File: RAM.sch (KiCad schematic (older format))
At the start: 1 part, among them IC1 EP4CE10F17

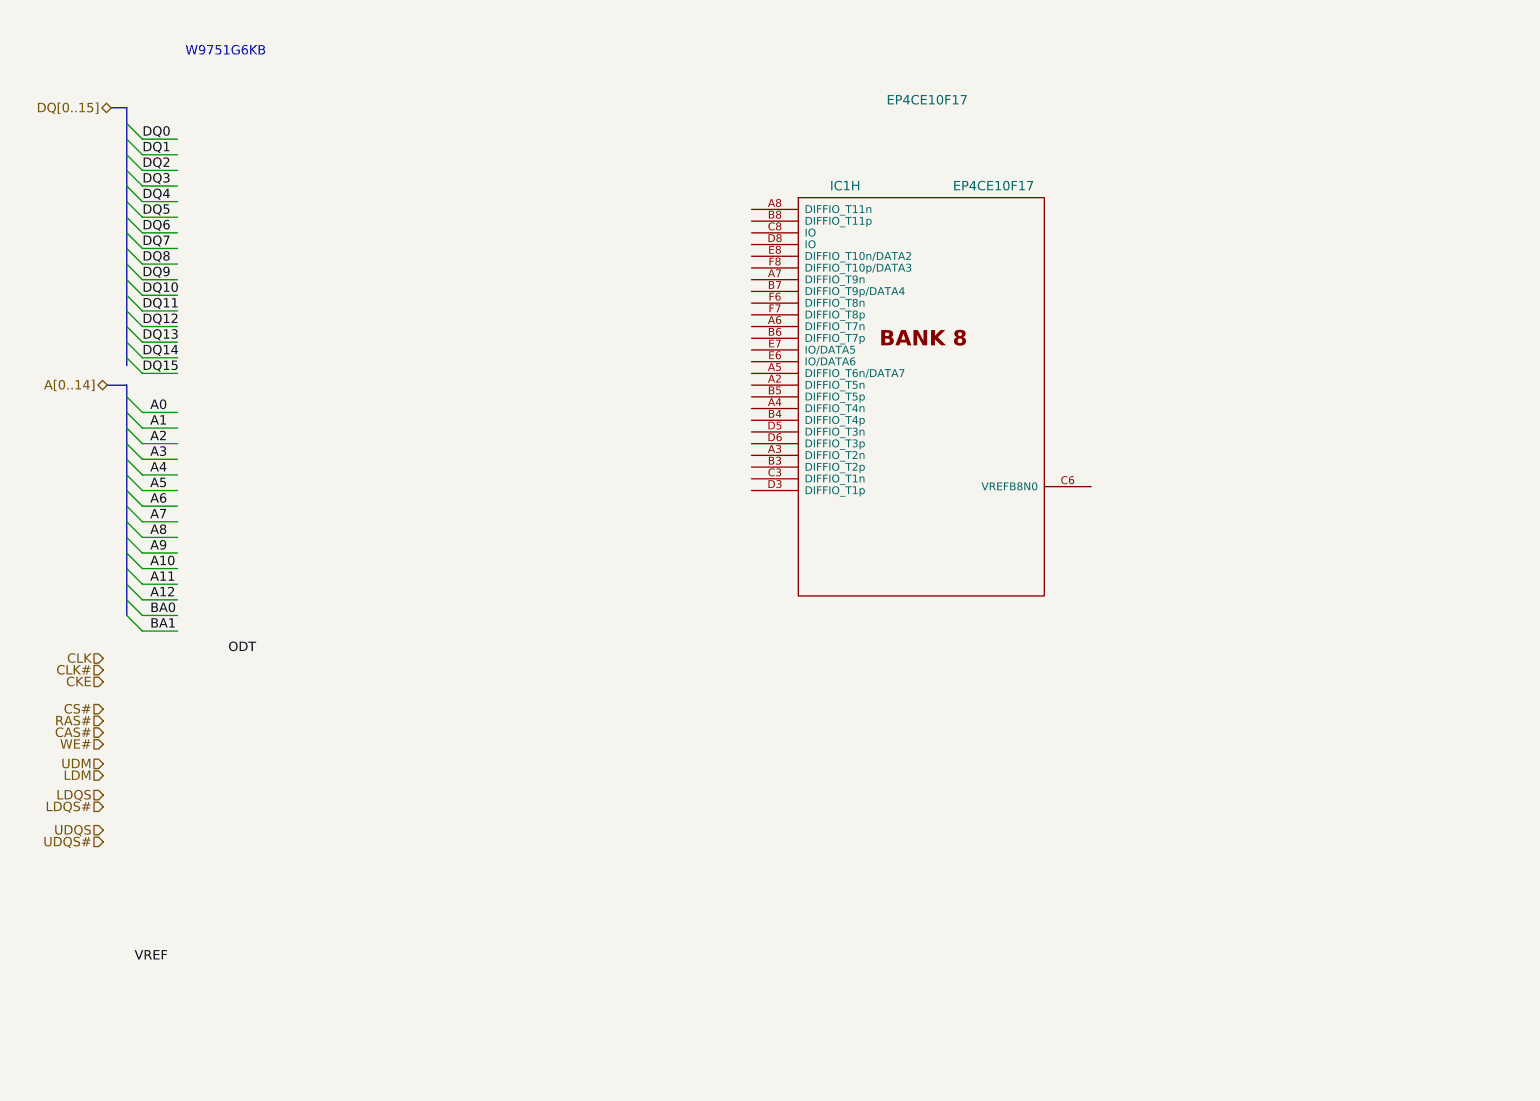
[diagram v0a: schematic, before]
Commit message: Start fitting DDR2
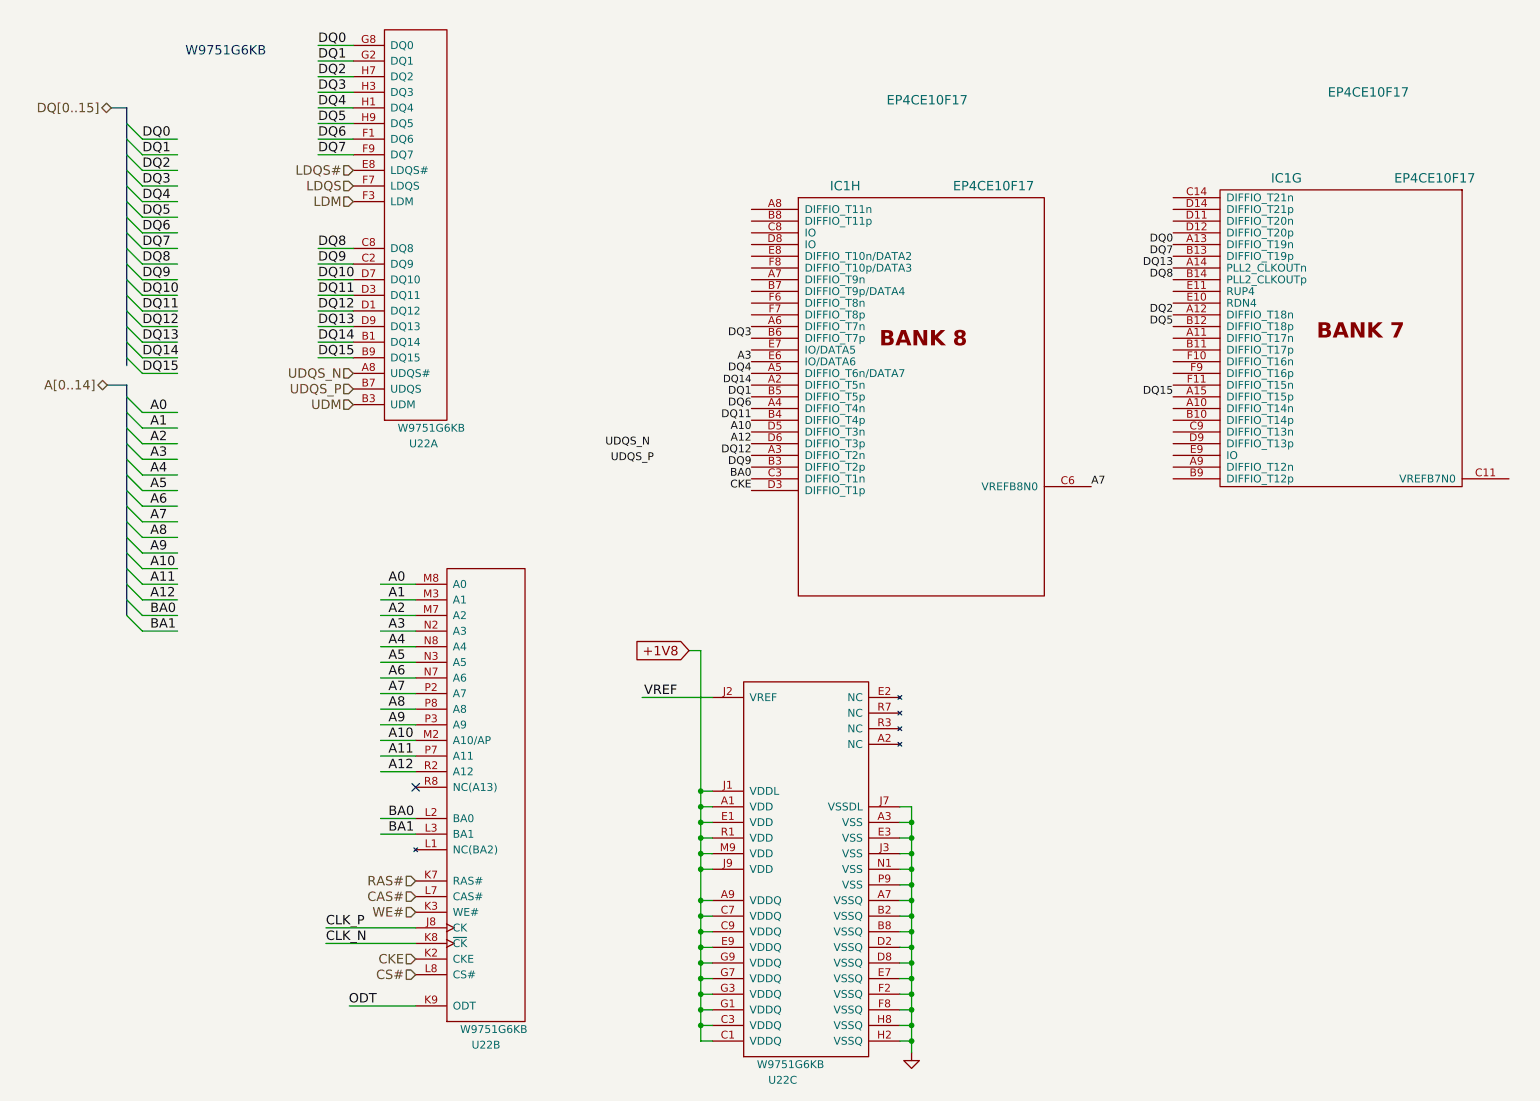
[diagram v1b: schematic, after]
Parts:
- added unit 7 of IC1
- added U22: W9751G6KB, Winbond:WBGA-84, symbol W9751G6KB
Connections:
- net labels added: +1V8, CLK_N, CLK_P, GND, UDQS_N, UDQS_P
- net labels removed: CLK, CLK#, UDQS, UDQS#
- wire segments 31 -> 101
- no-connect marks 0 -> 1

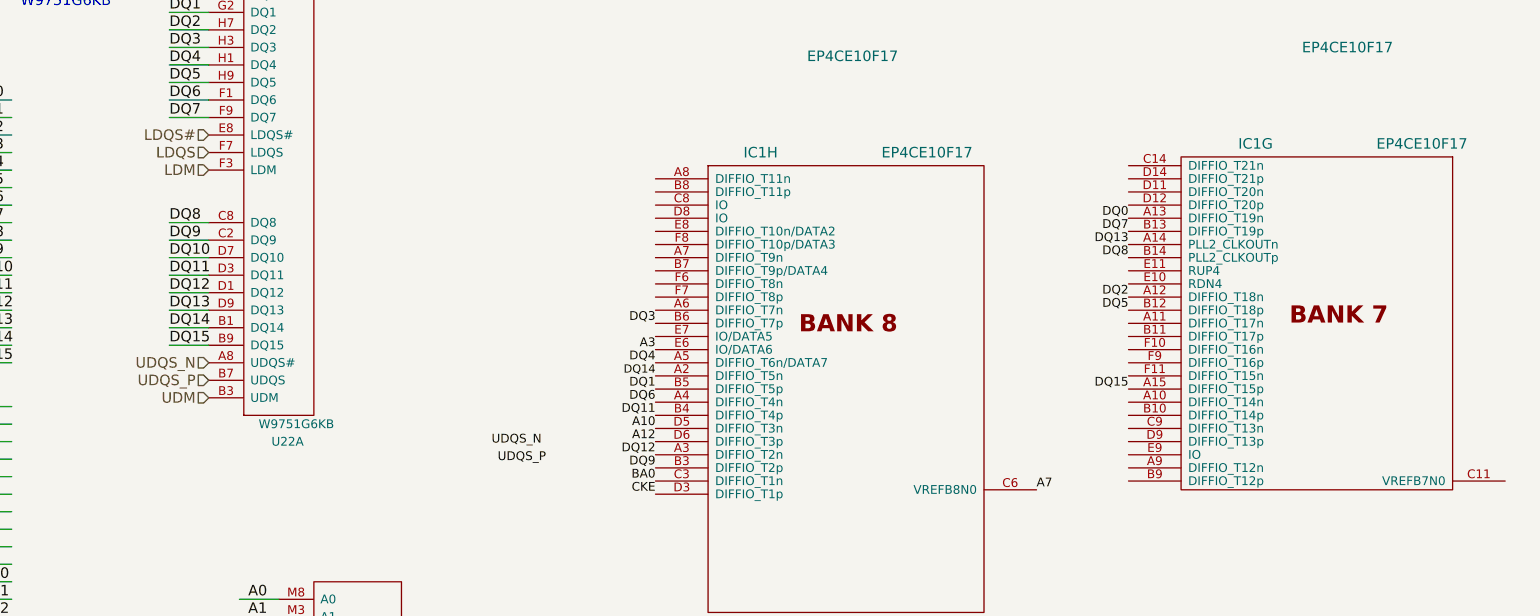
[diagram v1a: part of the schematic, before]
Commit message: DDR signals assignment and routing in progress
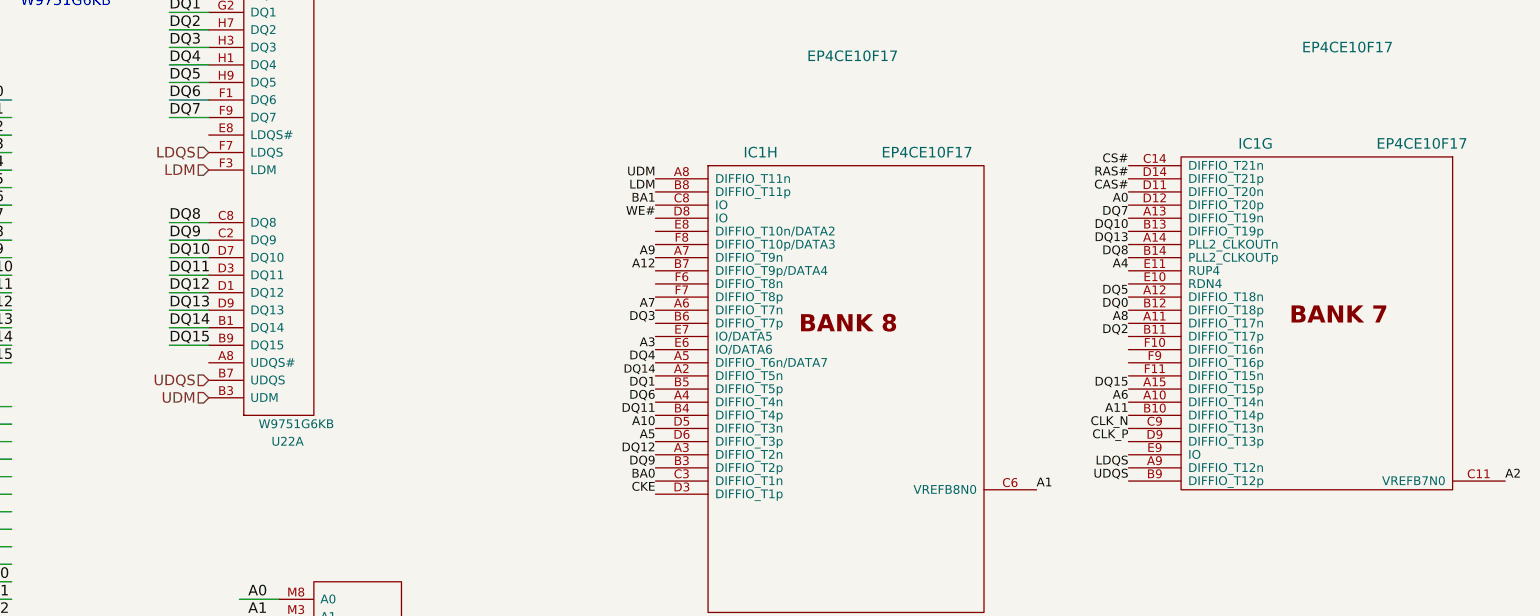
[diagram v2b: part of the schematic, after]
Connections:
- net labels added: UDQS
- net labels removed: LDQS#, UDQS_N, UDQS_P
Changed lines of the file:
@@
 Text HLabel 2700 1750 0    60   Input ~ 0
 LDQS
-Text HLabel 2700 1650 0    60   Input ~ 0
-LDQS#
 Text HLabel 2700 3050 0    60   Input ~ 0
-UDQS_P
-Text HLabel 2700 2950 0    60   Input ~ 0
-UDQS_N
+UDQS
 $Comp
 L EP4CE10F17 IC1
@@
 BA1
 $Comp
-L GND #PWR131
+L GND #PWR0131
 U 1 1 5882F59D
 P 6275 7300
-F 0 "#PWR131" H 6275 7050 50  0001 C CNN
+F 0 "#PWR0131" H 6275 7050 50  0001 C CNN
 F 1 "GND" H 6275 7150 50  0001 C CNN
 F 2 "" H 6275 7300 50  0000 C CNN
@@
 Wire Wire Line
 	3100 7000 2675 7000
-Text Label 4625 3525 2    50   ~ 0
-UDQS_P
-Text Label 4600 3425 2    50   ~ 0
-UDQS_N
 Wire Wire Line
 	3100 6500 2525 6500
@@
 Text Label 7950 2275 2    50   ~ 0
 DQ13
-Text Label 7950 2200 2    50   ~ 0
+Text Label 7950 2125 2    50   ~ 0
 DQ7
-Text Label 7950 2125 2    50   ~ 0
+Text Label 7950 2650 2    50   ~ 0
 DQ0
-Text Label 7950 2650 2    50   ~ 0
+Text Label 7950 2575 2    50   ~ 0
 DQ5
-Text Label 7950 2575 2    50   ~ 0
+Text Label 7950 2800 2    50   ~ 0
 DQ2
 Text Label 5250 3700 2    50   ~ 0
@@
 Text Label 5250 2875 2    50   ~ 0
 A3
+Text Label 5250 2650 2    50   ~ 0
+A7
+Text Label 5250 2425 2    50   ~ 0
+A12
+Text Label 7950 2200 2    50   ~ 0
+DQ10
+Text Label 7950 2725 2    50   ~ 0
+A8
+Text Label 7950 3250 2    50   ~ 0
+A11
+Text Label 5250 2350 2    50   ~ 0
+A9
+Text Label 7950 3325 2    50   ~ 0
+CLK_N
+Text Label 7950 3400 2    50   ~ 0
+CLK_P
+Text Label 7950 1975 2    50   ~ 0
+CAS#
+Text Label 10100 3625 0    50   ~ 0
+A2
+Text Label 5250 3400 2    50   ~ 0
+A5
 Text Label 7425 3675 0    50   ~ 0
-A7
-Text Label 5250 3400 2    50   ~ 0
-A12
+A1
+Text Label 5250 2050 2    50   ~ 0
+BA1
+Text Label 5250 2125 2    50   ~ 0
+WE#
+Text Label 5250 1975 2    50   ~ 0
+LDM
+Text Label 5250 1900 2    50   ~ 0
+UDM
+Text Label 7950 3625 2    50   ~ 0
+UDQS
+Text Label 7950 3550 2    50   ~ 0
+LDQS
+Text Label 7950 3175 2    50   ~ 0
+A6
+Text Label 7950 2425 2    50   ~ 0
+A4
+Text Label 7950 2050 2    50   ~ 0
+A0
+Text Label 7950 1825 2    50   ~ 0
+CS#
+Text Label 7950 1900 2    50   ~ 0
+RAS#
 $EndSCHEMATC

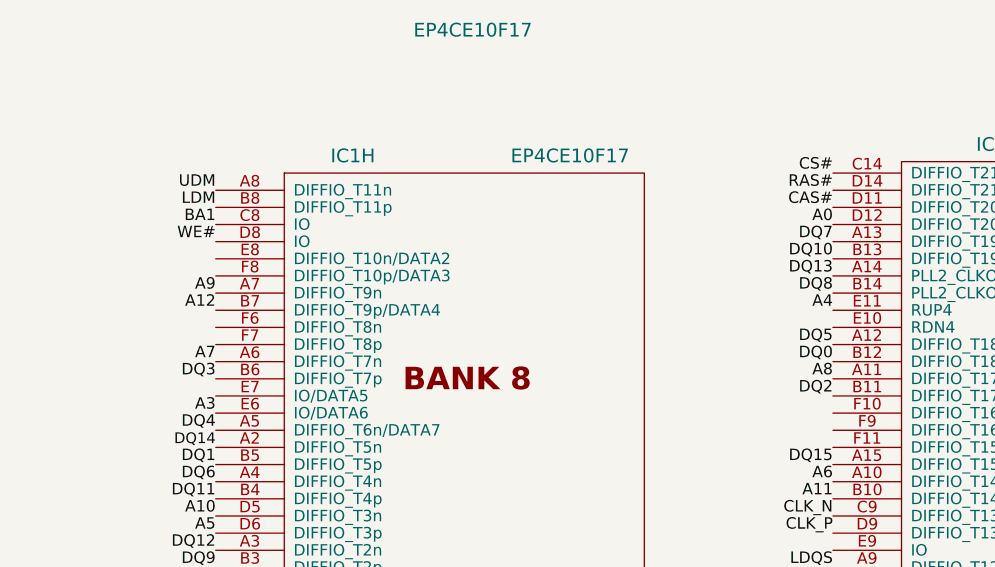
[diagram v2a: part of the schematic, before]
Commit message: DDR bottom signals length matched
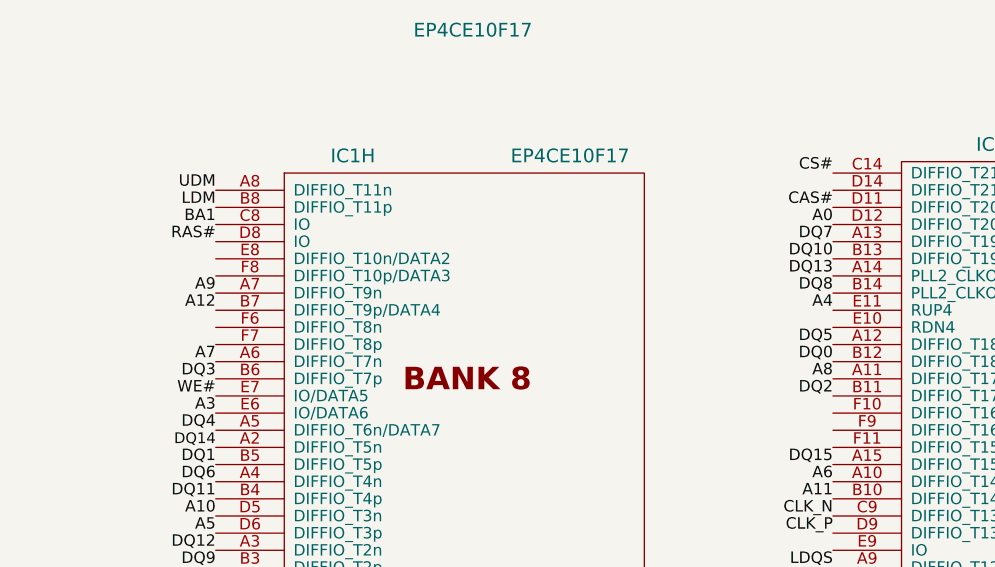
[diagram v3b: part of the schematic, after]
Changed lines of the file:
@@
 Text Label 5250 2050 2    50   ~ 0
 BA1
-Text Label 5250 2125 2    50   ~ 0
+Text Label 5250 2800 2    50   ~ 0
 WE#
 Text Label 5250 1975 2    50   ~ 0
@@
 Text Label 7950 1825 2    50   ~ 0
 CS#
-Text Label 7950 1900 2    50   ~ 0
+Text Label 5250 2125 2    50   ~ 0
 RAS#
 $EndSCHEMATC

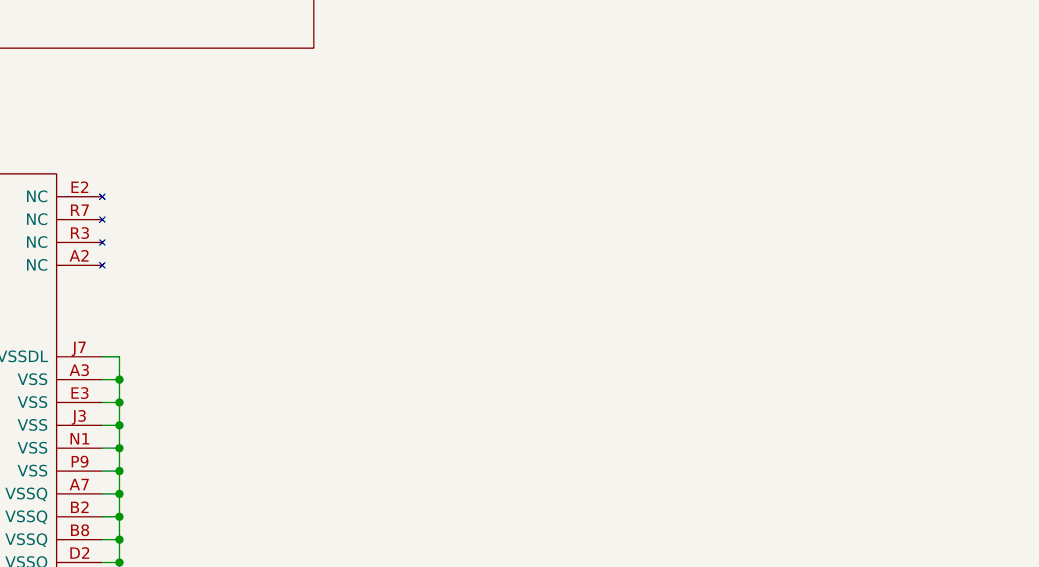
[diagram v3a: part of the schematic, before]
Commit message: Bottom 1V8 caps in progress
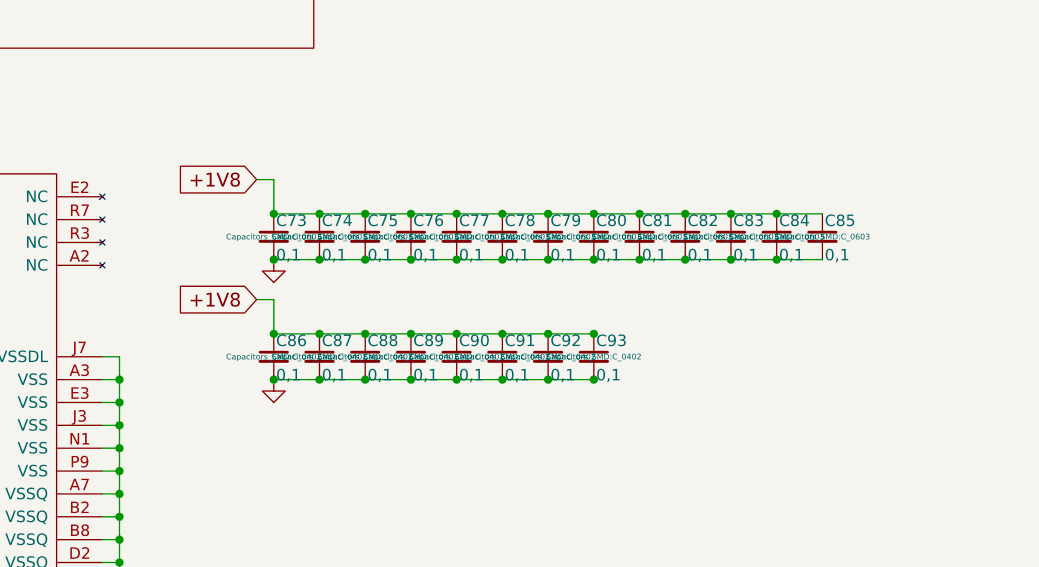
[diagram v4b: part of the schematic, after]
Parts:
- added C73, C74, C75, C76, C77, C78, C79, C80, C81, C82, C83, C84, C85: 0,1, Capacitors_SMD:C_0603, symbol C_Small
- added C86, C87, C88, C89, C90, C91, C92, C93: 0,1, Capacitors_SMD:C_0402, symbol C_Small
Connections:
- wire segments 101 -> 109

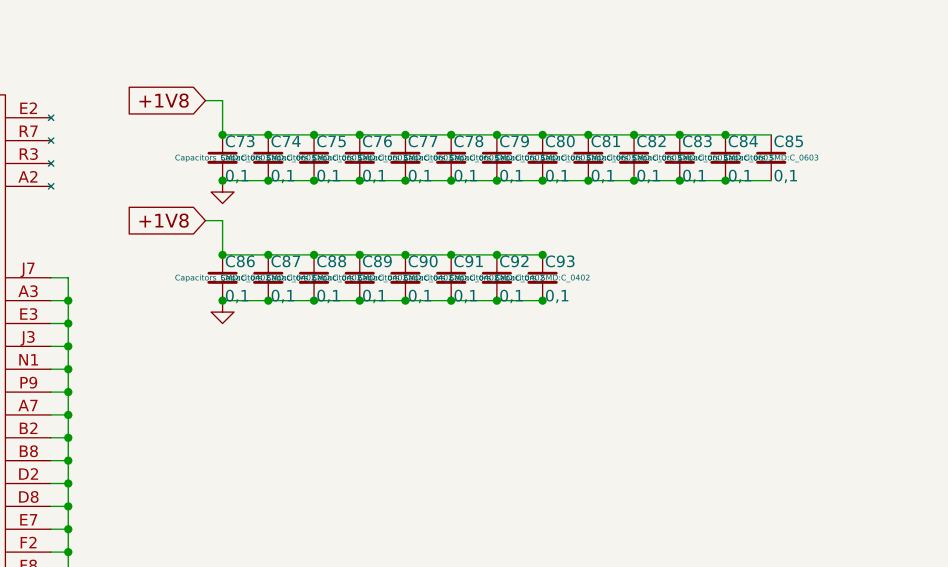
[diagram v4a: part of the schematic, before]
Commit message: DDR2 bottom decoupling
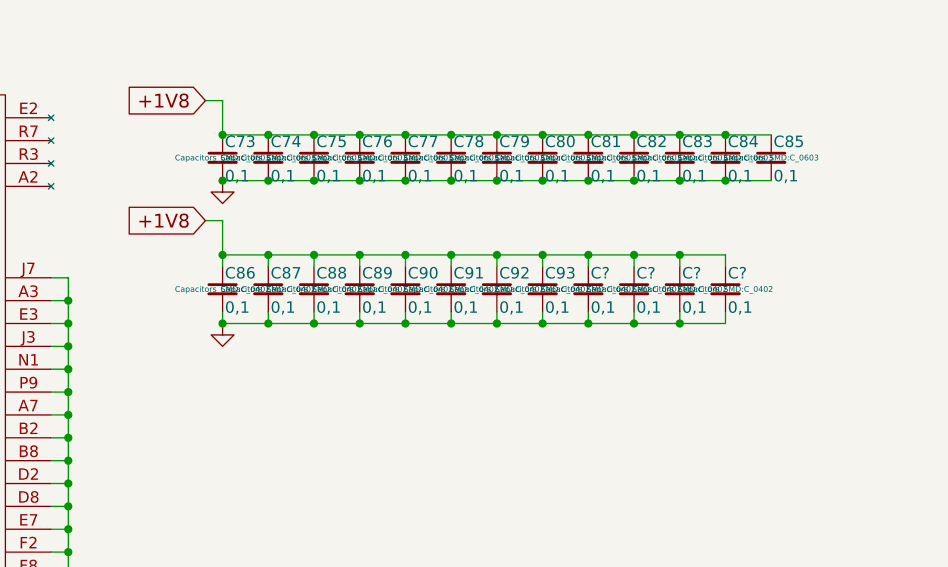
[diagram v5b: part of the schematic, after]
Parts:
- added C? (x4): 0,1, Capacitors_SMD:C_0402, symbol C_Small
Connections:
- wire segments 109 -> 132
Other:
- moved on the sheet: C86, C87, C88, C89, C90, C91, C92, C93
